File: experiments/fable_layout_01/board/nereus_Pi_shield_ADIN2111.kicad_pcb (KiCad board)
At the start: 6 copper layers, 46 x 65 mm, 138 parts, among them J1 Raspberry_Pi_2_3, J5 SM02B-GHS-TB, T1 74930000, T2 74930000, U1 ADIN2111BCPZ, U10 LMR51430YDDCR, U11 TPS26621DRCR, U2 AP22913CN4-7, U3 AP22913CN4-7, U4 INA232AIDDFR, U5 LMR51430YDDCR, U6 TPS62840YBGR, Y1 ABM11W-25.0000MHZ-6-K1Z-T3

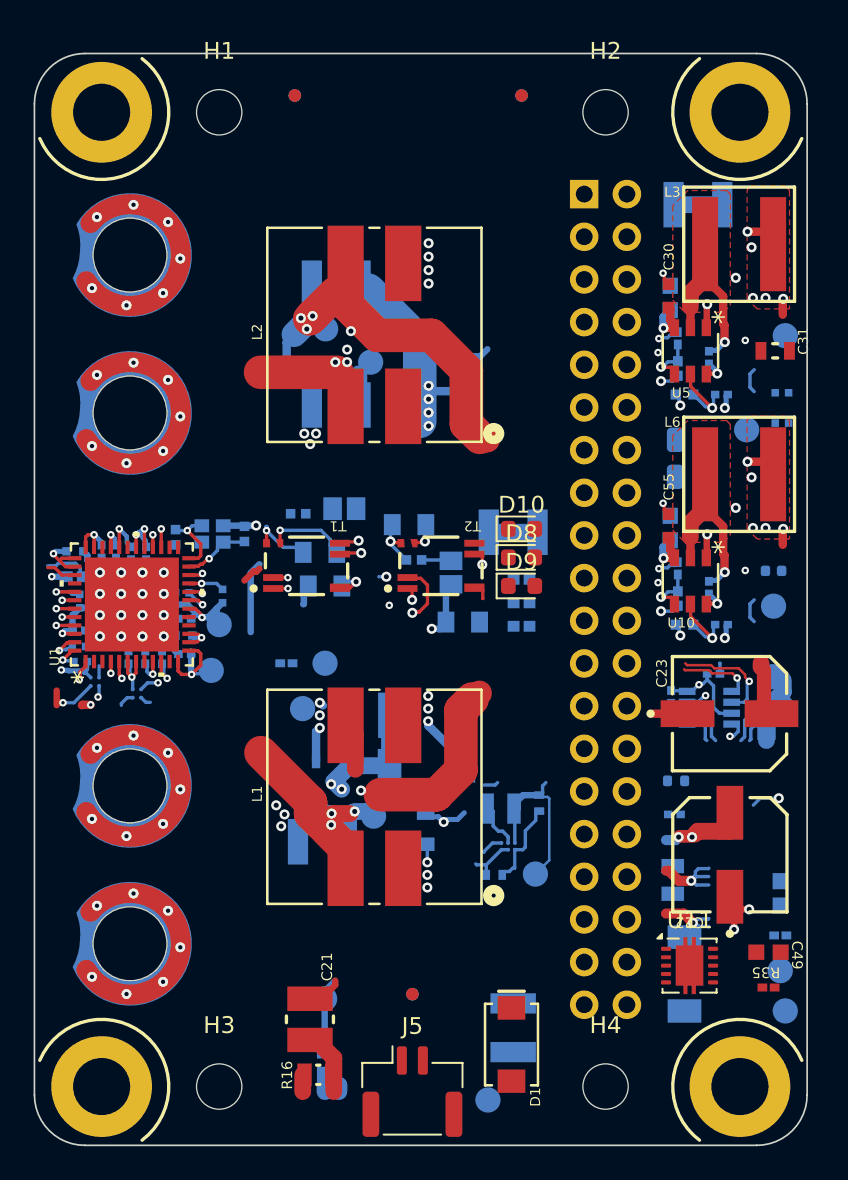
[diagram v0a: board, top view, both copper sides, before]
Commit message: fable layout 01 M4: planes, grid router, 216 -> 2 open (U3 3V3 link; J1 no-connect pair), zone fill
Co-Authored-By: Claude Fable 5.1 <noreply@anthropic.com>
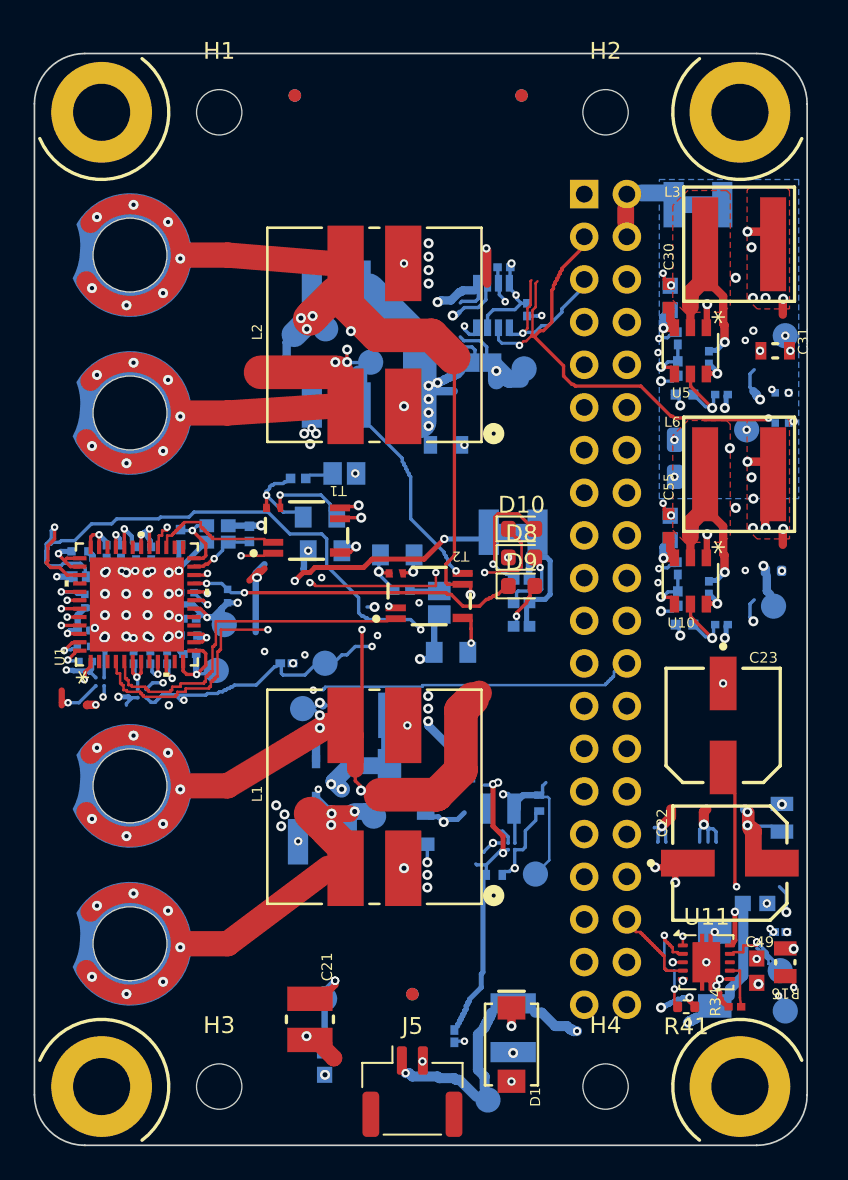
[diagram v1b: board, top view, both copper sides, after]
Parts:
- R34, R41: moved to F.Cu
- R35: moved to B.Cu
- moved R16 28.6 mm to (37.2, 54.1), turned to 90 degrees
- moved C15 27.4 mm to (20.4, 12.7), turned to 0 degrees
- moved R8 27.2 mm to (19.1, 18.4), turned to 180 degrees
- moved U4 27.2 mm to (19.8, 15.0), turned to -90 degrees
- moved R7 24.4 mm to (21.8, 15.2), turned to -90 degrees
- moved TP22 23.6 mm to (21.6, 18.8), turned to 90 degrees
- moved R35 18.9 mm to (17.5, 58.5), turned to 90 degrees
- moved R41 13.5 mm to (31.3, 56.8), turned to 180 degrees
- moved R34 12.0 mm to (34.2, 56.8)
- moved R15 7.48 mm to (37.0, 45.5)
- moved C26 4.37 mm to (17.0, 23.3), turned to 0 degrees
- moved C19 2.10 mm to (10.9, 25.0)
- moved R14 2.10 mm to (8.20, 25.3)
- moved T1 2.10 mm to (8.70, 28.4)
- moved C16 2.10 mm to (9.50, 27.6)
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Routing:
- net 3V3: track 28.5 -> 85.0 mm, vias 6 -> 15
- net /Top-Level Schematic/~{ADIN_INT}: track 4.48 -> 50.7 mm, vias 0 -> 2
- net /Top-Level Schematic/~{ADIN_CS}: track 1.67 -> 41.1 mm, vias 1 -> 2
- net /Top-Level Schematic/ADIN_MISO: track 1.69 -> 38.6 mm, vias 1 -> 3
- net /Top-Level Schematic/ADIN_PWR: track 19.4 -> 56.1 mm, vias 1 -> 3
- net /Top-Level Schematic/ADIN_MOSI: track 2.11 -> 38.4 mm, vias 1 -> 3
- net /Top-Level Schematic/ADIN/~{ADIN_P2_LED1}: track 1.72 -> 36.6 mm, vias 1 -> 3
- net /Top-Level Schematic/ADIN_SCK: track 1.60 -> 33.8 mm, vias 1 -> 2
- net VBUS_OUT: track 0.00 -> 27.7 mm, vias 0 -> 4
- net 1V8: track 11.3 -> 37.7 mm, vias 0 -> 3
- net /Top-Level Schematic/~{ADIN_RST}: track 15.2 -> 39.7 mm
- net /Top-Level Schematic/~{PAYLOAD_FAULT}: track 0.00 -> 24.1 mm, vias 0 -> 3
- net /Top-Level Schematic/BM1_N: track 36.1 -> 59.5 mm, vias 11 -> 12
- net /Top-Level Schematic/I2C1_SDA: track 6.45 -> 29.8 mm, vias 1 -> 2
- net /Top-Level Schematic/BM1_P: track 36.8 -> 59.5 mm, vias 12 -> 13
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- added copper zone on In4.Cu, net (none)
- added copper zone on B.Cu, net /Top-Level Schematic/5V_PI
- added copper zone on In4.Cu, net /Top-Level Schematic/PoDL/Power Monitor/P_IN
- added copper zone on In4.Cu, net 3V3
- added copper zone on In2.Cu, net GND
- added copper zone on In4.Cu, net VBUS

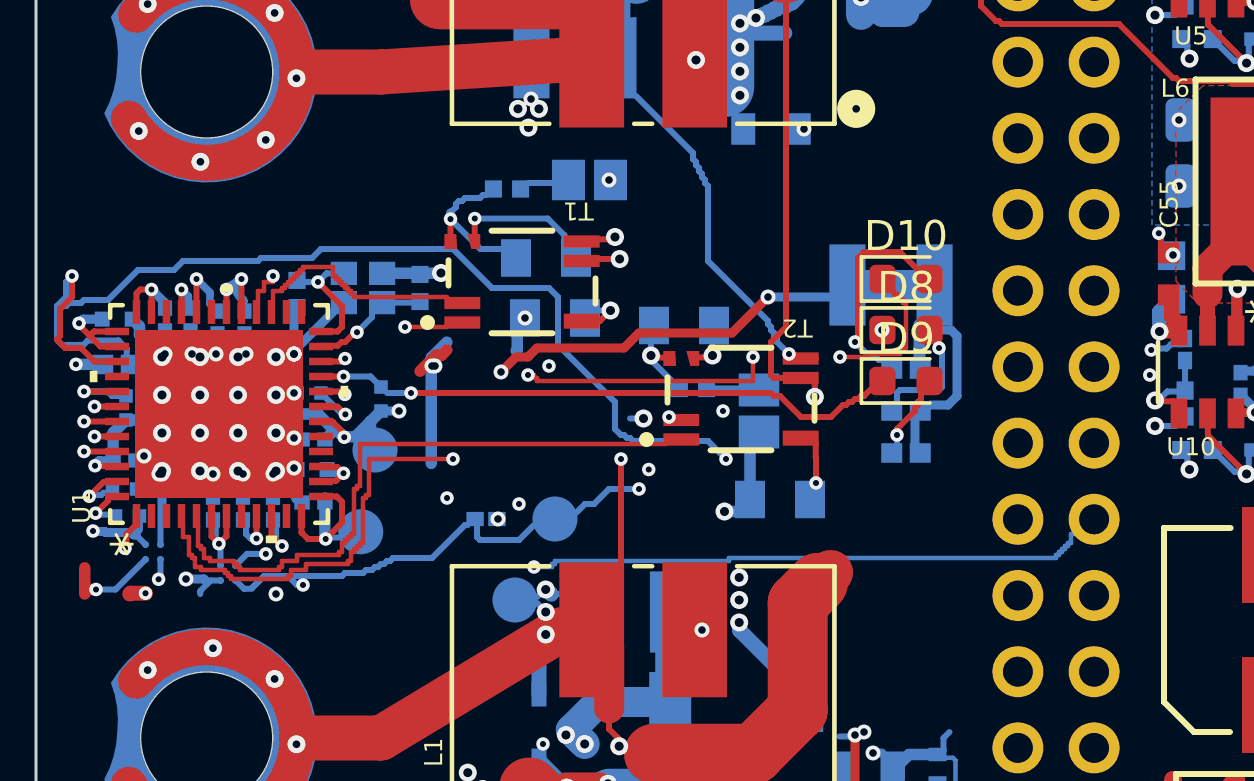
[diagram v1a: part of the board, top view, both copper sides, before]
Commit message: fable layout 01 M5: DRC exclusion table, rule check, renders, REPORT.md
Co-Authored-By: Claude Fable 5.1 <noreply@anthropic.com>
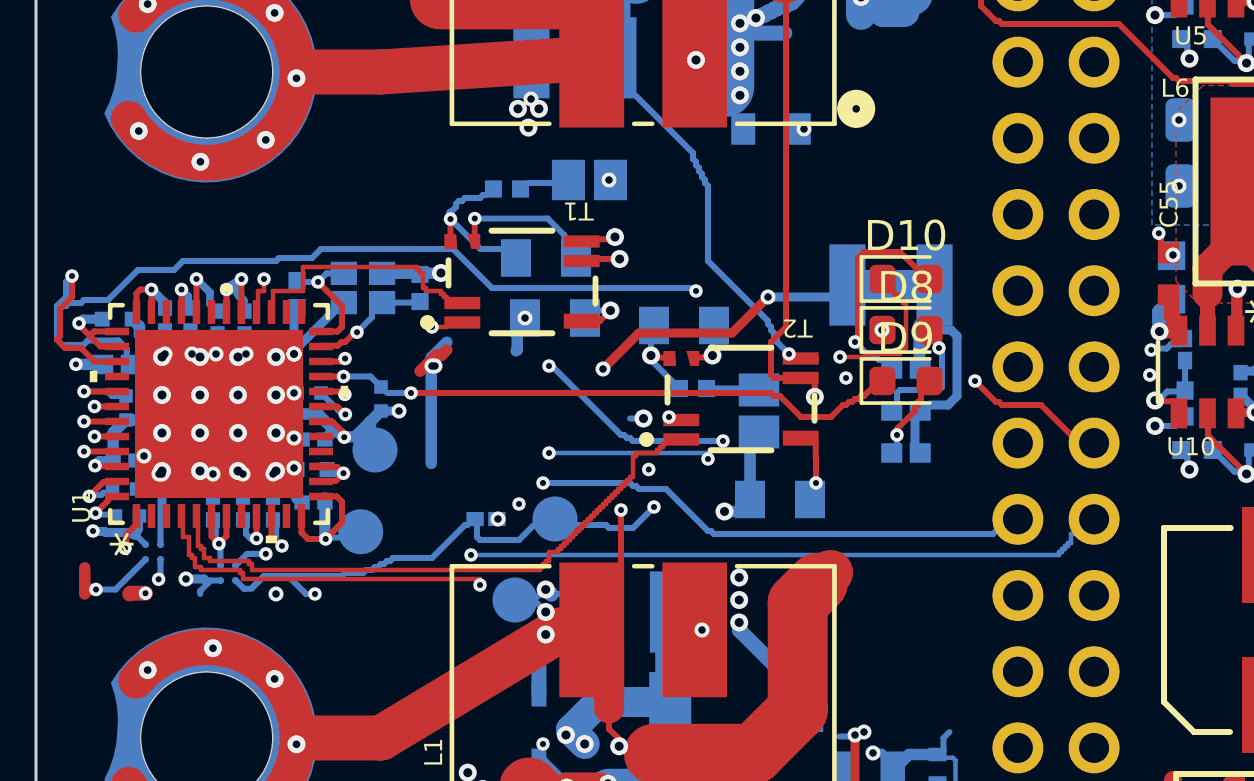
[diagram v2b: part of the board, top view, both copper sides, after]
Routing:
- net /Top-Level Schematic/~{ADIN_INT}: track 50.7 -> 48.2 mm, vias 2 -> 4
- net /Top-Level Schematic/ADIN_MOSI: track 38.4 -> 37.2 mm

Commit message: fable layout 01 S7.b round 1: QE F1-F6/N1-N5 fixed in the pipeline; 3V3 closed, 1 open (J1 by design)
- planes 0.25 + bus netclass 0.35; router hole map (no hole-to-hole / co-located vias)
- stitching into the filled copper; dangling copper trimmed by DRC's own items (tools/dangling.py)
- 3V3 escape via lookup fixed and routed; insert copper check; REPORT/LOG rewritten from fresh outputs
- QE report saved to experiments/fable_layout_01/qe/S7b_round1.md

Co-Authored-By: Claude Fable 5.1 <noreply@anthropic.com>
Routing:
- net 3V3: track 85.0 -> 108.2 mm, vias 15 -> 17
- net /Top-Level Schematic/BM1_P: track 59.5 -> 41.3 mm, vias 13 -> 12
- net /Top-Level Schematic/~{ADIN_RST}: track 39.7 -> 27.1 mm
- net /Top-Level Schematic/ADIN_PWR: track 56.1 -> 44.0 mm
- net /Top-Level Schematic/BM2_N: track 46.3 -> 36.2 mm
- net /Top-Level Schematic/BM1_N: track 59.5 -> 51.0 mm
- net /Top-Level Schematic/BM2_P: track 59.1 -> 53.3 mm
- net GND: track 75.5 -> 70.2 mm, vias 110 -> 85
- net VBUS: track 38.5 -> 34.2 mm, vias 25 -> 22
- net /Top-Level Schematic/PoDL/Power Monitor/P_IN: track 19.0 -> 15.1 mm
- net /Top-Level Schematic/I2C1_SDA: track 29.8 -> 26.5 mm
- net /Top-Level Schematic/I2C1_SCL: track 22.0 -> 18.7 mm
- net /Top-Level Schematic/~{ADIN_INT}: track 48.2 -> 50.7 mm, vias 4 -> 2
- net Net-(U11-UVLO): track 6.50 -> 4.90 mm
- net /Top-Level Schematic/ADIN_SCK: track 34.0 -> 32.6 mm
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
